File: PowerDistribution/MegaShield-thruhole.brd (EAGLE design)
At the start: 109.2 x 53.3 mm, 36 parts, among them IC1 TLE5205-2, IC2 TLE5205-2, IC3 TLE5205-2, J10 DCJ0202

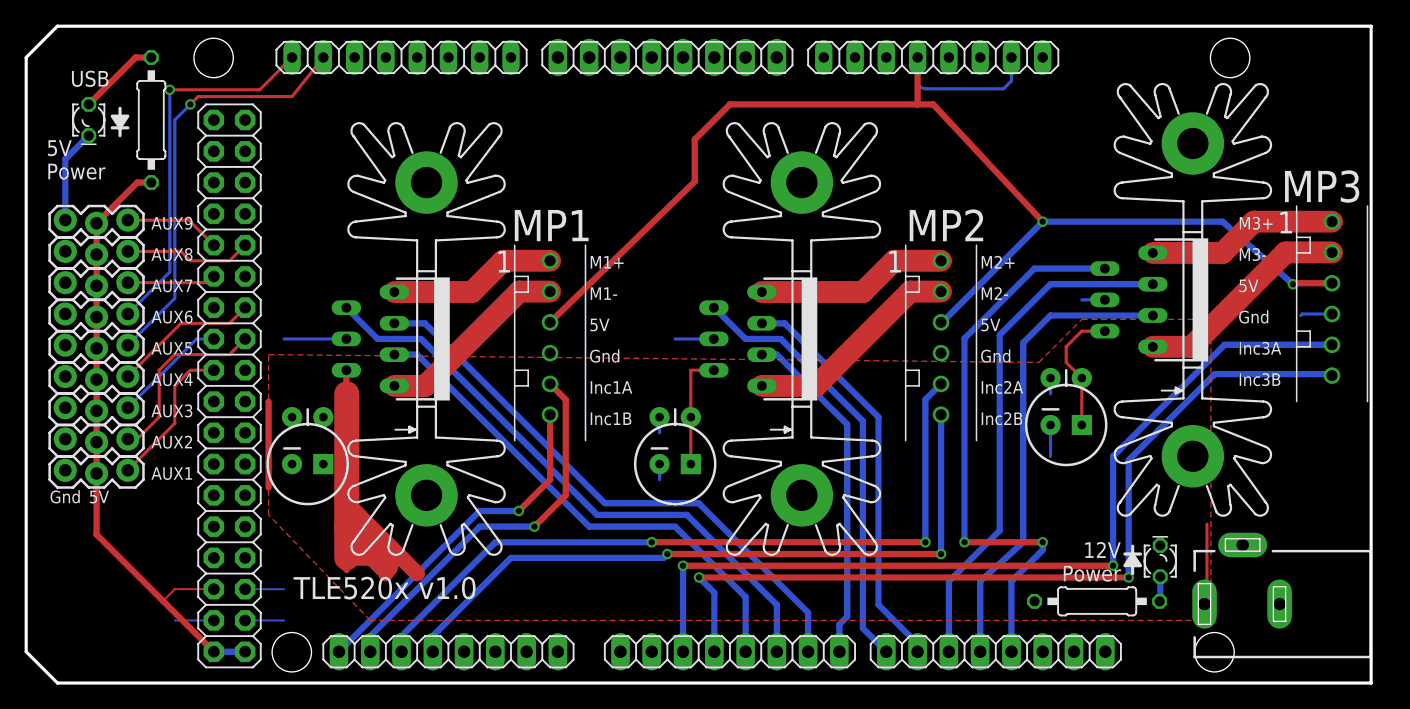
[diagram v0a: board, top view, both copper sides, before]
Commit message: clean up and correct pin spacing
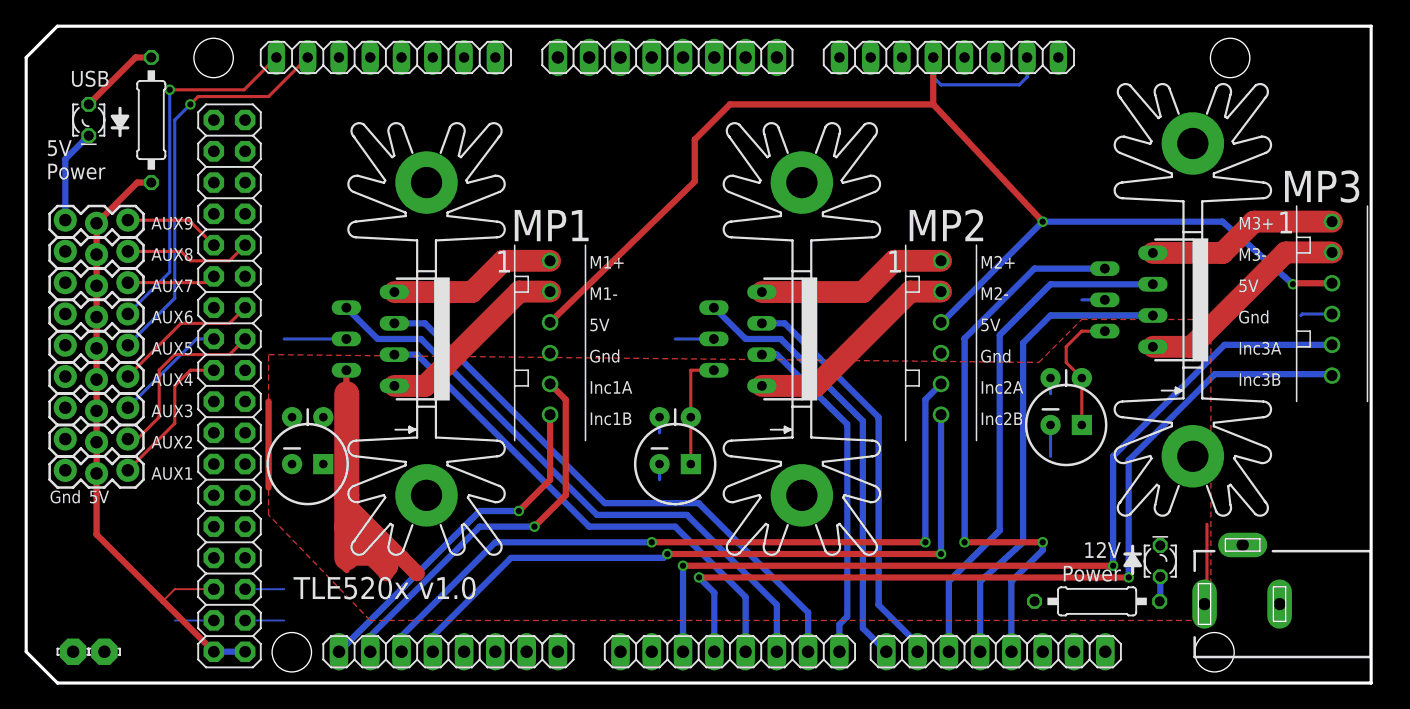
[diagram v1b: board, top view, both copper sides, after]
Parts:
- added TP1, TP2: LSP10, solpad:LSP10
- moved POWER 1.27 mm to (74.9, 50.8)
- moved ADCH 1.27 mm to (29.2, 50.8)
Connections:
- net GND: now also TP1.MP, TP2.MP
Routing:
- net AUX5: track 34.2 -> 32.8 mm
- net AUX6: track 30.6 -> 29.4 mm
- net 5V: track 157.9 -> 157.2 mm
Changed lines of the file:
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@@
 <setting verticaltext="up"/>
 </settings>
-<grid distance="0.025" unitdist="inch" unit="inch" style="lines" multiple="1" display="yes" altdistance="0.0125" altunitdist="inch" altunit="inch"/>
+<grid distance="0.1" unitdist="inch" unit="inch" style="lines" multiple="1" display="yes" altdistance="0.0125" altunitdist="inch" altunit="inch"/>
 <layers>
 <layer number="1" name="Top" color="12" fill="1" visible="yes" active="yes"/>
@@
 <attribute name="VALUE" x="1.905" y="34.29" size="1.27" layer="27"/>
 </element>
-<element name="ADCH" library="SmartPrj" package="1X08" value="8x1F-H8.5" x="30.48" y="50.8" smashed="yes" rot="R180">
-<attribute name="NAME" x="40.7162" y="48.9712" size="1.27" layer="25" ratio="10" rot="R180" display="off"/>
-<attribute name="VALUE" x="40.64" y="53.975" size="1.27" layer="27" rot="R180" display="off"/>
+<element name="ADCH" library="SmartPrj" package="1X08" value="8x1F-H8.5" x="29.21" y="50.8" smashed="yes" rot="R180">
+<attribute name="NAME" x="39.4462" y="48.9712" size="1.27" layer="25" ratio="10" rot="R180" display="off"/>
+<attribute name="VALUE" x="39.37" y="53.975" size="1.27" layer="27" rot="R180" display="off"/>
 </element>
-<element name="POWER" library="SmartPrj" package="1X08" value="8x1F-H8.5" x="73.66" y="50.8" smashed="yes" rot="R180">
-<attribute name="NAME" x="83.8962" y="48.9712" size="1.27" layer="25" ratio="10" rot="R180" display="off"/>
-<attribute name="VALUE" x="83.82" y="53.975" size="1.27" layer="27" rot="R180" display="off"/>
+<element name="POWER" library="SmartPrj" package="1X08" value="8x1F-H8.5" x="74.93" y="50.8" smashed="yes" rot="R180">
+<attribute name="NAME" x="85.1662" y="48.9712" size="1.27" layer="25" ratio="10" rot="R180" display="off"/>
+<attribute name="VALUE" x="85.09" y="53.975" size="1.27" layer="27" rot="R180" display="off"/>
+</element>
+<element name="TP1" library="solpad" library_urn="urn:adsk.eagle:library:364" package="LSP10" package3d_urn="urn:adsk.eagle:package:26501/1" value="LSP10" x="3.81" y="2.54" smashed="yes">
+<attribute name="NAME" x="2.54" y="3.81" size="1.27" layer="25" ratio="10" display="off"/>
+<attribute name="VALUE" x="3.81" y="2.794" size="0.0254" layer="27" display="off"/>
+</element>
+<element name="TP2" library="solpad" library_urn="urn:adsk.eagle:library:364" package="LSP10" package3d_urn="urn:adsk.eagle:package:26501/1" value="LSP10" x="6.35" y="2.54" smashed="yes">
+<attribute name="NAME" x="5.08" y="3.81" size="1.27" layer="25" ratio="10" display="off"/>
+<attribute name="VALUE" x="6.35" y="2.794" size="0.0254" layer="27" display="off"/>
 </element>
 </elements>
@@
 <wire x1="17.78" y1="5.08" x2="20.955" y2="5.08" width="0.1524" layer="16"/>
 <wire x1="17.78" y1="7.62" x2="20.955" y2="7.62" width="0.1524" layer="16"/>
+<contactref element="TP1" pad="MP"/>
+<contactref element="TP2" pad="MP"/>
 </signal>
 <signal name="INC2B">
@@
 <wire x1="54.2925" y1="40.72" x2="54.2925" y2="44.1325" width="0.508" layer="1"/>
 <wire x1="54.2925" y1="44.1325" x2="57.15" y2="46.99" width="0.508" layer="1"/>
-<wire x1="57.15" y1="46.99" x2="72.39" y2="46.99" width="0.508" layer="1"/>
-<wire x1="72.39" y1="46.99" x2="73.66" y2="46.99" width="0.508" layer="1"/>
+<wire x1="57.15" y1="46.99" x2="73.66" y2="46.99" width="0.508" layer="1"/>
 <wire x1="73.66" y1="46.99" x2="82.55" y2="37.465" width="0.508" layer="1"/>
 <via x="82.55" y="37.465" extent="1-16" drill="0.508"/>
@@
 <contactref element="POWER" pad="5"/>
 <contactref element="POWER" pad="2"/>
-<wire x1="72.39" y1="50.8" x2="72.39" y2="46.99" width="0.508" layer="1"/>
-<wire x1="80.01" y1="50.8" x2="80.01" y2="48.895" width="0.254" layer="16"/>
-<wire x1="80.01" y1="48.895" x2="79.375" y2="48.26" width="0.254" layer="16"/>
-<wire x1="73.025" y1="48.26" x2="72.39" y2="48.895" width="0.254" layer="16" curve="-90"/>
-<wire x1="72.39" y1="48.895" x2="72.39" y2="50.8" width="0.254" layer="16"/>
-<wire x1="79.375" y1="48.26" x2="73.025" y2="48.26" width="0.254" layer="16"/>
+<wire x1="73.66" y1="50.8" x2="73.66" y2="46.99" width="0.508" layer="1"/>
+<wire x1="81.28" y1="50.8" x2="81.28" y2="49.2125" width="0.254" layer="16"/>
+<wire x1="81.28" y1="49.2125" x2="80.645" y2="48.5775" width="0.254" layer="16"/>
+<wire x1="80.645" y1="48.5775" x2="74.295" y2="48.5775" width="0.254" layer="16"/>
+<wire x1="74.295" y1="48.5775" x2="73.66" y2="49.2125" width="0.254" layer="16"/>
+<wire x1="73.66" y1="49.2125" x2="73.66" y2="50.8" width="0.254" layer="16"/>
 <wire x1="15.24" y1="2.54" x2="11.1125" y2="6.6675" width="0.508" layer="1"/>
 <wire x1="11.1125" y1="6.6675" x2="5.715" y2="12.065" width="0.508" layer="1"/>
@@
 <wire x1="9.017" y1="40.64" x2="10.16" y2="40.64" width="0.508" layer="1"/>
 <contactref element="XIO" pad="6"/>
-<wire x1="15.24" y1="7.62" x2="12.7" y2="7.62" width="0.1524" layer="1"/>
-<wire x1="12.7" y1="7.62" x2="12.065" y2="7.62" width="0.1524" layer="1"/>
+<wire x1="15.24" y1="7.62" x2="12.065" y2="7.62" width="0.1524" layer="1"/>
 <wire x1="12.065" y1="7.62" x2="11.1125" y2="6.6675" width="0.1524" layer="1"/>
 <wire x1="10.16" y1="40.64" x2="42.545" y2="29.29" width="0" layer="19" extent="1-1"/>
@@
 <contactref element="J5" pad="3"/>
 <contactref element="ADCH" pad="7"/>
-<wire x1="24.13" y1="50.8" x2="21.59" y2="47.625" width="0.254" layer="1"/>
-<wire x1="21.59" y1="47.625" x2="13.97" y2="47.625" width="0.254" layer="1"/>
+<wire x1="22.86" y1="50.8" x2="19.685" y2="47.625" width="0.254" layer="1"/>
+<wire x1="19.685" y1="47.625" x2="13.97" y2="47.625" width="0.254" layer="1"/>
 <wire x1="13.97" y1="47.625" x2="13.335" y2="46.99" width="0.254" layer="1"/>
 <wire x1="13.335" y1="46.99" x2="12.065" y2="45.72" width="0.254" layer="16"/>
@@
 <wire x1="11.6586" y1="48.17570625" x2="11.6586" y2="33.3756" width="0.254" layer="16"/>
 <via x="11.6586" y="48.17570625" extent="1-16" drill="0.508"/>
-<wire x1="11.6586" y1="48.17570625" x2="18.96570625" y2="48.17570625" width="0.254" layer="1"/>
-<wire x1="18.96570625" y1="48.17570625" x2="21.59" y2="50.8" width="0.254" layer="1"/>
+<wire x1="11.6586" y1="48.17570625" x2="17.69570625" y2="48.17570625" width="0.254" layer="1"/>
+<wire x1="17.69570625" y1="48.17570625" x2="20.32" y2="50.8" width="0.254" layer="1"/>
 </signal>
 <signal name="N$3">

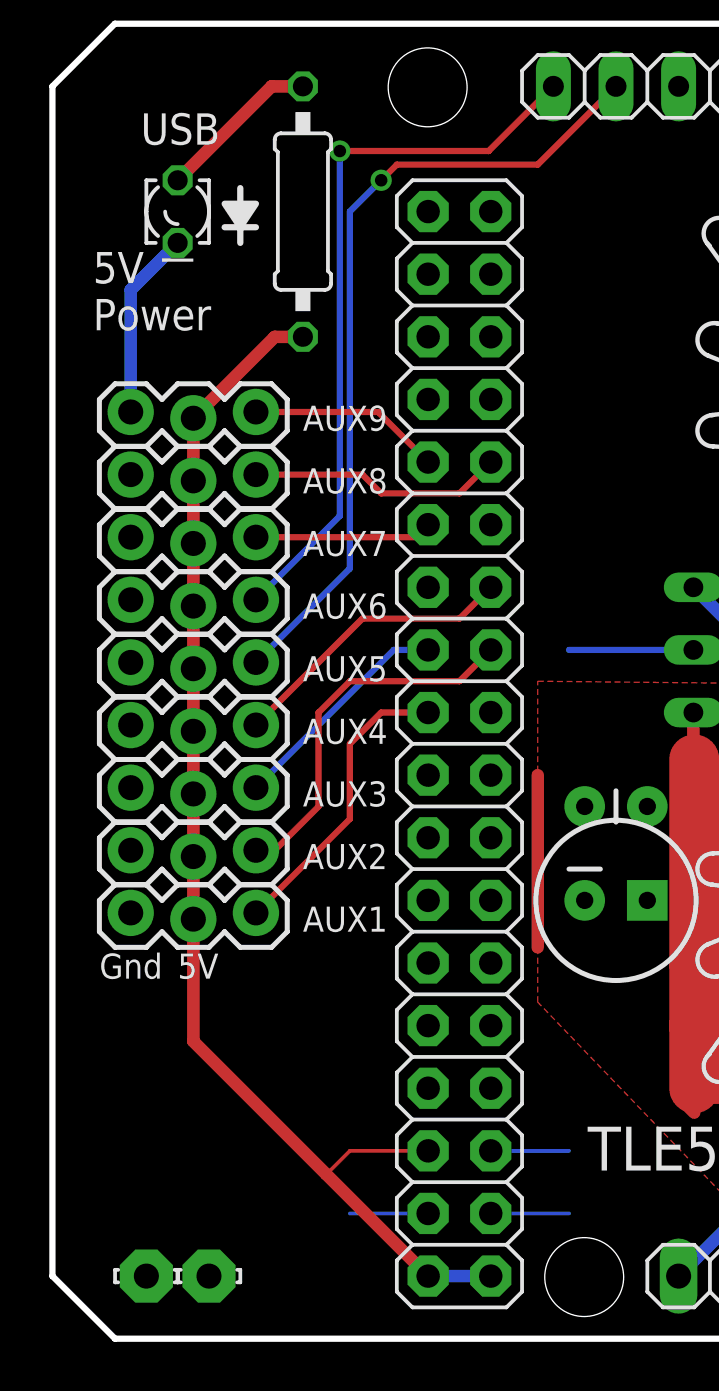
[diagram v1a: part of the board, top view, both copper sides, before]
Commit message: Move AUX conections to other source pins
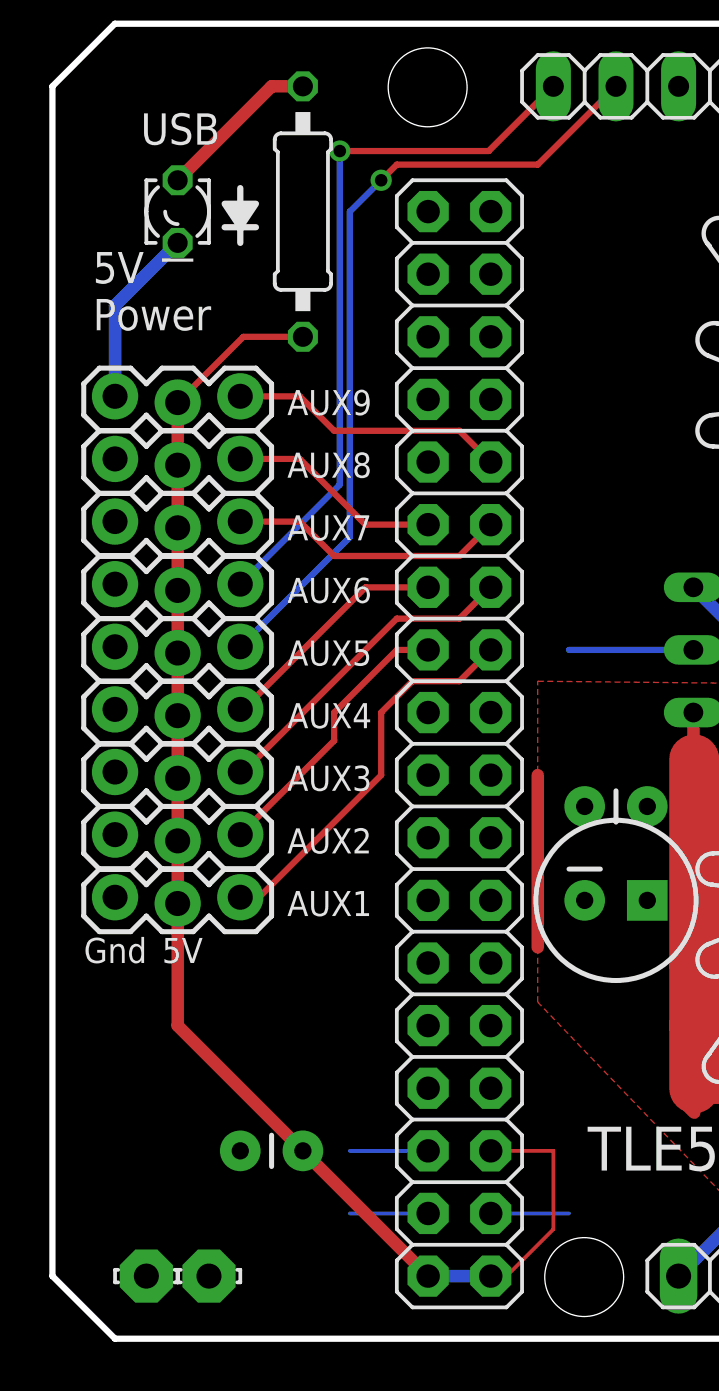
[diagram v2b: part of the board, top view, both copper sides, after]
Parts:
- added C7: 1uF, SparkFun:CAP-PTH-SMALL
- C2, C4, C6: value 100nF -> 0.1uF
- moved J7 0.90 mm to (2.54, 33.0)
- moved J8 0.90 mm to (2.54, 35.6)
- moved J1 0.90 mm to (2.54, 17.8)
- moved J2 0.90 mm to (2.54, 20.3)
- moved J5 0.90 mm to (2.54, 27.9)
- moved J6 0.90 mm to (2.54, 30.5)
- moved J3 0.90 mm to (2.54, 22.9)
- moved J4 0.90 mm to (2.54, 25.4)
- moved J9 0.90 mm to (2.54, 38.1)
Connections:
- removed net PL1: XIO.29
- net 5V: now also C7.1, XIO.5; no longer XIO.6
- net AUX1: now also XIO.21; no longer XIO.20
- net AUX2: now also XIO.22; no longer XIO.21
- net AUX3: now also XIO.23; no longer XIO.22
- net AUX4: now also XIO.24; no longer XIO.23
- net AUX7: now also XIO.25; no longer XIO.26
- net AUX8: now also XIO.26; no longer XIO.27
- net AUX9: now also XIO.27; no longer XIO.28
- net GND: now also C7.2, XIO.6; no longer XIO.5
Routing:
- net 5V: track 157.2 -> 163.0 mm
- net AUX3: track 9.30 -> 13.4 mm
- net AUX7: track 7.20 -> 11.3 mm
- net AUX2: track 15.1 -> 11.4 mm
- net AUX1: track 12.1 -> 15.8 mm
- net AUX9: track 7.83 -> 11.3 mm
- net AUX4: track 11.8 -> 9.85 mm
- net AUX8: track 10.4 -> 8.72 mm

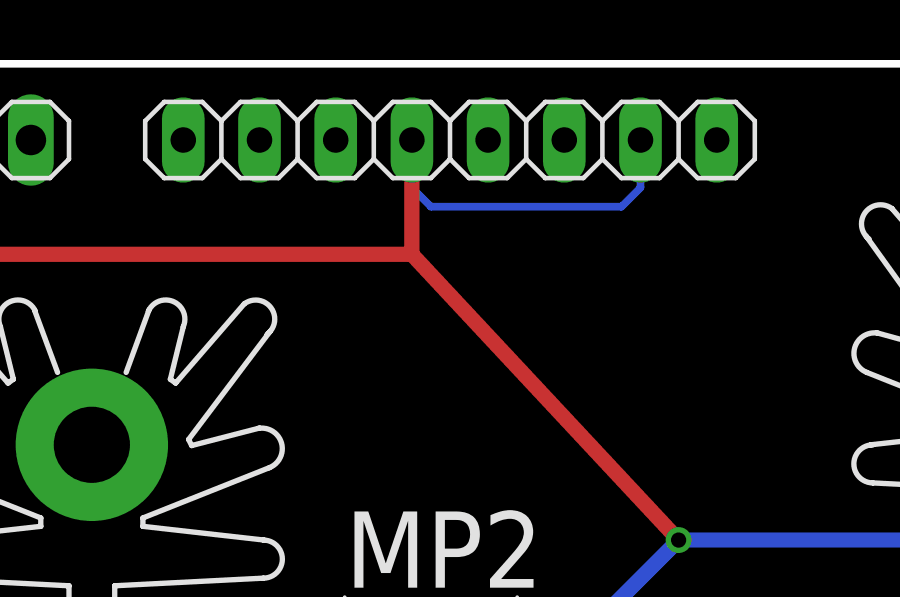
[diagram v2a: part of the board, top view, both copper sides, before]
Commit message: Add second 5V bypass cap
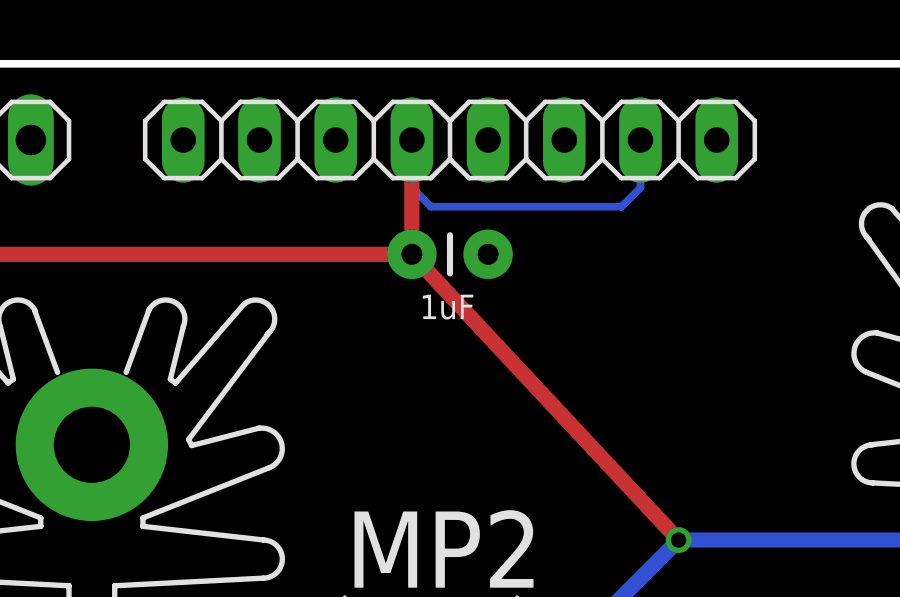
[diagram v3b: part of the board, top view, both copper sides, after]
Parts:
- added C8: 1uF, SparkFun:CAP-PTH-SMALL
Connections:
- net 5V: now also C8.1
- net GND: now also C8.2
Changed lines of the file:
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@@
 <attribute name="VALUE" x="8.509" y="9.271" size="0.8128" layer="27"/>
+</element>
+<element name="C8" library="SparkFun" package="CAP-PTH-SMALL" value="1uF" x="73.66" y="46.99" smashed="yes">
+<attribute name="NAME" x="74.168" y="48.26" size="0.8128" layer="25" display="off"/>
+<attribute name="VALUE" x="73.914" y="44.831" size="0.8128" layer="21"/>
 </element>
 </elements>
@@
 <wire x1="15.24" y1="7.62" x2="12.065" y2="7.62" width="0.1524" layer="16"/>
 <contactref element="C7" pad="2"/>
+<contactref element="C8" pad="2"/>
 </signal>
 <signal name="INC2B">
@@
 <wire x1="7.747" y1="40.64" x2="10.16" y2="40.64" width="0.254" layer="1"/>
 <contactref element="C7" pad="1"/>
+<contactref element="C8" pad="1"/>
 <wire x1="20.32" y1="7.62" x2="42.545" y2="29.29" width="0" layer="19" extent="1-1"/>
 <wire x1="10.16" y1="7.62" x2="15.24" y2="2.54" width="0" layer="19" extent="16-16"/>
